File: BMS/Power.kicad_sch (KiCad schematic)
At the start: 1 part, among them J18 Conn_01x02

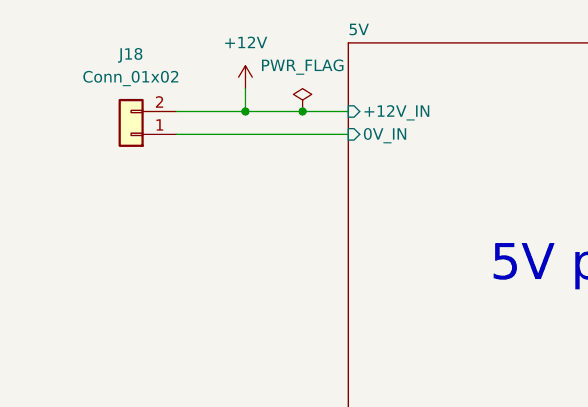
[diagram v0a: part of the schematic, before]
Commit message: Dodano layout drugiego bq79614, ukladu tlumaczącego z protokułu TI na UART oraz wstępnie poprowadzono pary różnicowe
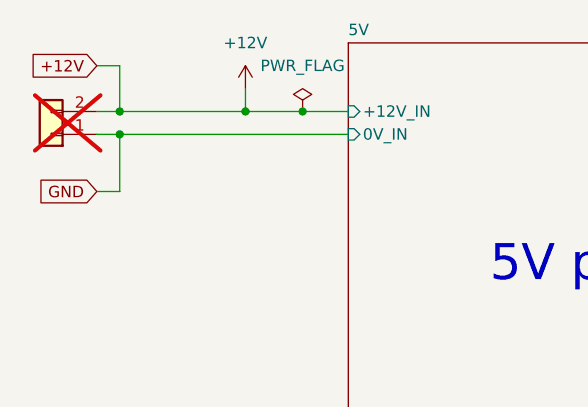
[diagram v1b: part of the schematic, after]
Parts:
- J18: now not fitted; now left out of the parts list
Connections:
- net 5V/0V_IN renamed GND
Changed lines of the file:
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@@
 	(paper "A4")
+	(junction
+		(at 24.13 43.18)
+		(diameter 0)
+		(color 0 0 0 0)
+	)
+	(junction
+		(at 24.13 40.64)
+		(diameter 0)
+		(color 0 0 0 0)
+	)
 	(junction
 		(at 44.45 40.64)
@@
 	(wire
 		(pts
+			(xy 24.13 49.53) (xy 24.13 43.18)
+		)
+		(stroke
+			(width 0)
+			(type default)
+		)
+	)
+	(wire
+		(pts
+			(xy 21.59 35.56) (xy 24.13 35.56)
+		)
+		(stroke
+			(width 0)
+			(type default)
+		)
+	)
+	(wire
+		(pts
 			(xy 130.81 44.45) (xy 171.45 44.45)
 		)
@@
 	(wire
 		(pts
-			(xy 30.48 40.64) (xy 38.1 40.64)
-		)
-		(stroke
-			(width 0)
-			(type default)
-		)
-	)
-	(wire
-		(pts
-			(xy 30.48 43.18) (xy 49.53 43.18)
+			(xy 21.59 49.53) (xy 24.13 49.53)
+		)
+		(stroke
+			(width 0)
+			(type default)
+		)
+	)
+	(wire
+		(pts
+			(xy 24.13 43.18) (xy 49.53 43.18)
+		)
+		(stroke
+			(width 0)
+			(type default)
+		)
+	)
+	(wire
+		(pts
+			(xy 24.13 35.56) (xy 24.13 40.64)
+		)
+		(stroke
+			(width 0)
+			(type default)
+		)
+	)
+	(wire
+		(pts
+			(xy 24.13 40.64) (xy 38.1 40.64)
+		)
+		(stroke
+			(width 0)
+			(type default)
+		)
+	)
+	(wire
+		(pts
+			(xy 21.59 40.64) (xy 24.13 40.64)
+		)
+		(stroke
+			(width 0)
+			(type default)
+		)
+	)
+	(wire
+		(pts
+			(xy 21.59 43.18) (xy 24.13 43.18)
 		)
 		(stroke
@@
 			(font
 				(size 4 4)
+			)
+		)
+	)
+	(global_label "+12V"
+		(shape input)
+		(at 21.59 35.56 180)
+		(fields_autoplaced yes)
+		(effects
+			(font
+				(size 1.27 1.27)
+			)
+			(justify right)
+		)
+		(property "Intersheetrefs" "${INTERSHEET_REFS}"
+			(at 13.5248 35.56 0)
+			(effects
+				(font
+					(size 1.27 1.27)
+				)
+				(justify right)
+				(hide yes)
+			)
+		)
+	)
+	(global_label "GND"
+		(shape input)
+		(at 21.59 49.53 180)
+		(fields_autoplaced yes)
+		(effects
+			(font
+				(size 1.27 1.27)
+			)
+			(justify right)
+		)
+		(property "Intersheetrefs" "${INTERSHEET_REFS}"
+			(at 14.7343 49.53 0)
+			(effects
+				(font
+					(size 1.27 1.27)
+				)
+				(justify right)
+				(hide yes)
 			)
 		)
@@
 	(symbol
 		(lib_id "Connector_Generic:Conn_01x02")
-		(at 25.4 43.18 180)
+		(at 16.51 43.18 180)
 		(unit 1)
-		(exclude_from_sim no)
-		(in_bom yes)
-		(on_board yes)
-		(dnp no)
+		(exclude_from_sim yes)
+		(in_bom no)
+		(on_board no)
+		(dnp yes)
 		(fields_autoplaced yes)
 		(property "Reference" "J18"
-			(at 25.4 34.29 0)
-			(effects
-				(font
-					(size 1.27 1.27)
-				)
+			(at 16.51 34.29 0)
+			(effects
+				(font
+					(size 1.27 1.27)
+				)
+				(hide yes)
 			)
 		)
 		(property "Value" "Conn_01x02"
-			(at 25.4 36.83 0)
-			(effects
-				(font
-					(size 1.27 1.27)
-				)
+			(at 16.51 36.83 0)
+			(effects
+				(font
+					(size 1.27 1.27)
+				)
+				(hide yes)
 			)
 		)
 		(property "Footprint" "footrpint:HARWIN_M80-5000000M1-02-PM1-00-000"
-			(at 25.4 43.18 0)
+			(at 16.51 43.18 0)
 			(effects
 				(font
@@
 		)
 		(property "Datasheet" "https://www.harwin.com/products/M80-5000000M1-02-PM1-00-000"
-			(at 25.4 43.18 0)
+			(at 16.51 43.18 0)
 			(effects
 				(font
@@
 		)
 		(property "Description" "Generic connector, single row, 01x02, script generated (kicad-library-utils/schlib/autogen/connector/)"
-			(at 24.892 46.482 0)
-			(effects
-				(font
+			(at 16.002 46.482 0)
+			(effects
+				(font

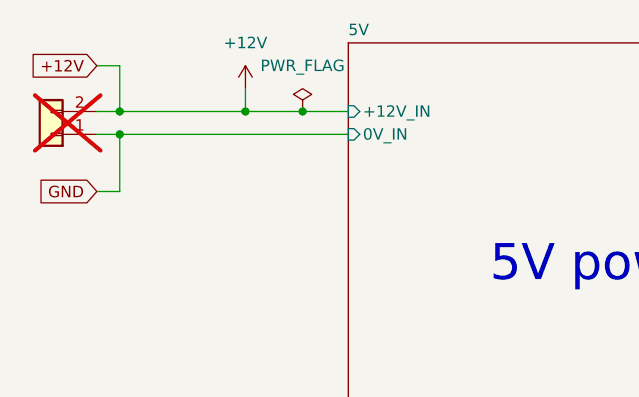
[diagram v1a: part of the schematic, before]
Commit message: Iteracja 1.0 gotowa, teraz sprawdzenie i zmiany kosmetyczne
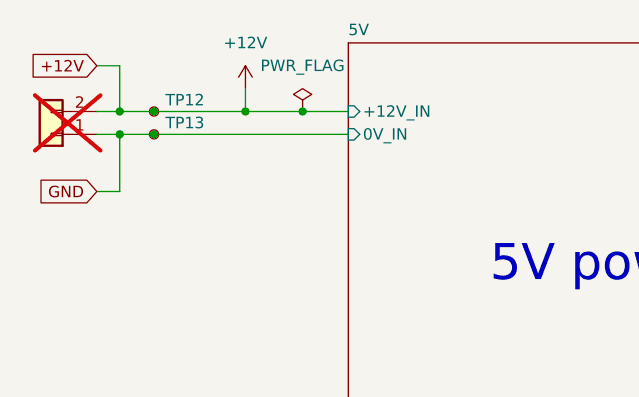
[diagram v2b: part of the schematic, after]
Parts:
- added TP12, TP13: TestPoint_Small, TestPoint:TestPoint_Pad_D1.0mm, symbol Connector:TestPoint_Small
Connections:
- net +12V: now also TP12.1
- net GND: now also TP13.1
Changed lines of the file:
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@@
 (kicad_sch
-	(version 20231120)
+	(version 20250114)
 	(generator "eeschema")
-	(generator_version "8.0")
+	(generator_version "9.0")
 	(paper "A4")
+	(text "Zasilacz z 110V na 12V "
+		(exclude_from_sim no)
+		(at 140.716 108.458 0)
+		(effects
+			(font
+				(size 10 10)
+			)
+		)
+	)
+	(text "Będzie zewnętrzny"
+		(exclude_from_sim no)
+		(at 138.938 125.73 0)
+		(effects
+			(font
+				(size 10 10)
+			)
+		)
+	)
+	(text "5V power supply\n"
+		(exclude_from_sim no)
+		(at 88.138 57.658 0)
+		(effects
+			(font
+				(size 4 4)
+			)
+		)
+	)
+	(text "3.3V power supply\n"
+		(exclude_from_sim no)
+		(at 215.9 54.356 0)
+		(effects
+			(font
+				(size 4 4)
+			)
+		)
+	)
 	(junction
 		(at 24.13 43.18)
@@
 	)
 	(junction
+		(at 27.94 43.18)
+		(diameter 0)
+		(color 0 0 0 0)
+	)
+	(junction
 		(at 24.13 40.64)
+		(diameter 0)
+		(color 0 0 0 0)
+	)
+	(junction
+		(at 27.94 40.64)
 		(diameter 0)
 		(color 0 0 0 0)
@@
 	(wire
 		(pts
-			(xy 24.13 43.18) (xy 49.53 43.18)
+			(xy 24.13 43.18) (xy 27.94 43.18)
 		)
 		(stroke
@@
 	(wire
 		(pts
-			(xy 24.13 40.64) (xy 38.1 40.64)
+			(xy 27.94 43.18) (xy 49.53 43.18)
+		)
+		(stroke
+			(width 0)
+			(type default)
+		)
+	)
+	(wire
+		(pts
+			(xy 24.13 40.64) (xy 27.94 40.64)
+		)
+		(stroke
+			(width 0)
+			(type default)
+		)
+	)
+	(wire
+		(pts
+			(xy 27.94 40.64) (xy 38.1 40.64)
 		)
 		(stroke
@@
 			(width 0)
 			(type default)
-		)
-	)
-	(text "Zasilacz z 110V na 12V "
-		(exclude_from_sim no)
-		(at 140.716 108.458 0)
-		(effects
-			(font
-				(size 10 10)
-			)
-		)
-	)
-	(text "Będzie zewnętrzny"
-		(exclude_from_sim no)
-		(at 138.938 125.73 0)
-		(effects
-			(font
-				(size 10 10)
-			)
-		)
-	)
-	(text "5V power supply\n"
-		(exclude_from_sim no)
-		(at 88.138 57.658 0)
-		(effects
-			(font
-				(size 4 4)
-			)
-		)
-	)
-	(text "3.3V power supply\n"
-		(exclude_from_sim no)
-		(at 215.9 54.356 0)
-		(effects
-			(font
-				(size 4 4)
-			)
 		)
 	)
@@
 	)
 	(symbol
+		(lib_id "Connector:TestPoint_Small")
+		(at 27.94 40.64 0)
+		(unit 1)
+		(exclude_from_sim no)
+		(in_bom yes)
+		(on_board yes)
+		(dnp no)
+		(fields_autoplaced yes)
+		(property "Reference" "TP12"
+			(at 29.21 39.3699 0)
+			(effects
+				(font
+					(size 1.27 1.27)
+				)
+				(justify left)
+			)
+		)
+		(property "Value" "TestPoint_Small"
+			(at 29.21 41.9099 0)
+			(effects
+				(font
+					(size 1.27 1.27)
+				)
+				(justify left)
+				(hide yes)
+			)
+		)
+		(property "Footprint" "TestPoint:TestPoint_Pad_D1.0mm"
+			(at 33.02 40.64 0)
+			(effects
+				(font
+					(size 1.27 1.27)
+				)
+				(hide yes)
+			)
+		)
+		(property "Datasheet" "~"
+			(at 33.02 40.64 0)
+			(effects
+				(font
+					(size 1.27 1.27)
+				)
+				(hide yes)
+			)
+		)
+		(property "Description" "test point"
+			(at 27.94 40.64 0)
+			(effects
+				(font
+					(size 1.27 1.27)
+				)
+				(hide yes)
+			)
+		)
+		(pin "1"
+		)
+		(instances
+			(project "BMS"
+				(path "/26289bb6-56bc-4ca1-b1a2-18d58d1afdf5/b306fb08-ef5e-4bf5-8efa-c4e5200f566a"
+					(reference "TP12")
+					(unit 1)
+				)
+			)
+		)
+	)
+	(symbol
+		(lib_id "Connector:TestPoint_Small")
+		(at 27.94 43.18 0)
+		(unit 1)
+		(exclude_from_sim no)
+		(in_bom yes)
+		(on_board yes)
+		(dnp no)
+		(fields_autoplaced yes)
+		(property "Reference" "TP13"
+			(at 29.21 41.9099 0)
+			(effects
+				(font
+					(size 1.27 1.27)
+				)
+				(justify left)
+			)
+		)
+		(property "Value" "TestPoint_Small"
+			(at 29.21 44.4499 0)
+			(effects
+				(font
+					(size 1.27 1.27)
+				)
+				(justify left)
+				(hide yes)
+			)
+		)
+		(property "Footprint" "TestPoint:TestPoint_Pad_D1.0mm"
+			(at 33.02 43.18 0)
+			(effects
+				(font
+					(size 1.27 1.27)
+				)
+				(hide yes)
+			)
+		)
+		(property "Datasheet" ""
+			(at 33.02 43.18 0)
+			(effects
+				(font
+					(size 1.27 1.27)
+				)
+				(hide yes)
+			)
+		)
+		(property "Description" ""
+			(at 27.94 43.18 0)
+			(effects
+				(font
+					(size 1.27 1.27)
+				)
+				(hide yes)
+			)
+		)
+		(pin "1"
+		)
+		(instances
+			(project "BMS"
+				(path "/26289bb6-56bc-4ca1-b1a2-18d58d1afdf5/b306fb08-ef5e-4bf5-8efa-c4e5200f566a"
+					(reference "TP13")
+					(unit 1)
+				)
+			)
+		)
+	)
+	(symbol
 		(lib_id "power:PWR_FLAG")
 		(at 44.45 40.64 0)
@@
 		(at 16.51 43.18 180)
 		(unit 1)
-		(exclude_from_sim yes)
+		(exclude_from_sim no)
 		(in_bom no)
 		(on_board no)
@@
 		(at 49.53 33.02)
 		(size 81.28 53.34)
+		(exclude_from_sim no)
+		(in_bom yes)
+		(on_board yes)
+		(dnp no)
 		(fields_autoplaced yes)
 		(stroke
@@
 		(at 171.45 33.02)
 		(size 81.28 53.34)
-		(fields_autoplaced yes)
-		(stroke
+		(exclude_from_sim no)
+		(in_bom yes)
+		(on_board yes)
+		(dnp no)
+		(fields_autoplaced yes)
+		(stroke
